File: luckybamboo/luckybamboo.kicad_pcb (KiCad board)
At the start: 4 copper layers, 70.7 x 53.3 mm, 153 parts, among them J1 NEIGHBOR1, J10 TEST_2P, J11 TEST_2P, J12 TEST_2P, J13 TEST_2P, J14 TEST_2P, J15 TEST_2P, J16 TEST_2P, J17 Conn_Coaxial, J18 Conn_Coaxial, J19 TEST_2P, J2 NEIGHBOR2, J20 TEST_2P, J21 TEST_2P, J22 TEST_2P, J23 TEST_2P, J24 TEST_2P, J25 TEST_2P, J26 TEST_2P, J27 TEST_2P, J28 TEST_2P, J29 TEST_2P, J3 Conn_01x08, J30 TEST_2P, J31 TEST_2P, J32 TEST_2P, J33 TEST_2P, J4 Conn_01x08, J5 Conn_01x08, J6 Conn_01x08, J7 BONUS_ROW, J8 TEST_2P, J9 TEST_2P, U1 ADF7242, U10 ADF7242_balun, U11 ADF7242_balun, U12 HHM2293A1, U13 BGA7H1N6, U14 ADF7242_balun, U15 ADF7242_balun, U16 ADF7242_balun, U17 ADF7242_balun, U2 ADF7242, U3 ADF7242, U4 ADF7242, U5 SKY13322, U6 HHM2293A1, U7 HHM2293A1, U8 ADF7242_balun, U9 ADF7242_balun, X1 XTAL4PIN, X2 XTAL4PIN, X3 XTAL4PIN, X4 XTAL4PIN

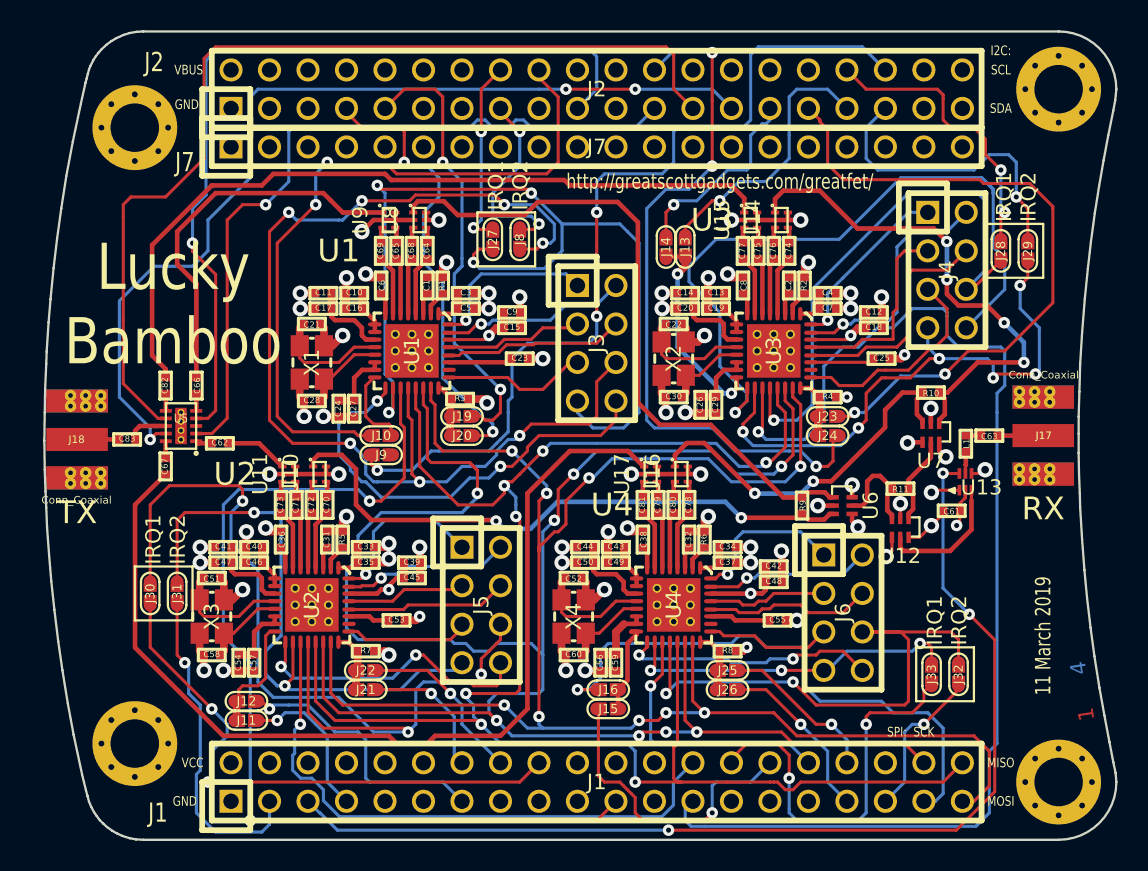
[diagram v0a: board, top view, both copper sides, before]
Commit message: Lucky Bamboo: Rerouted RX RF signals and rearranged schematic to be consistent with layout. Gladiolus: Routed incomplete signal near TX transistor.
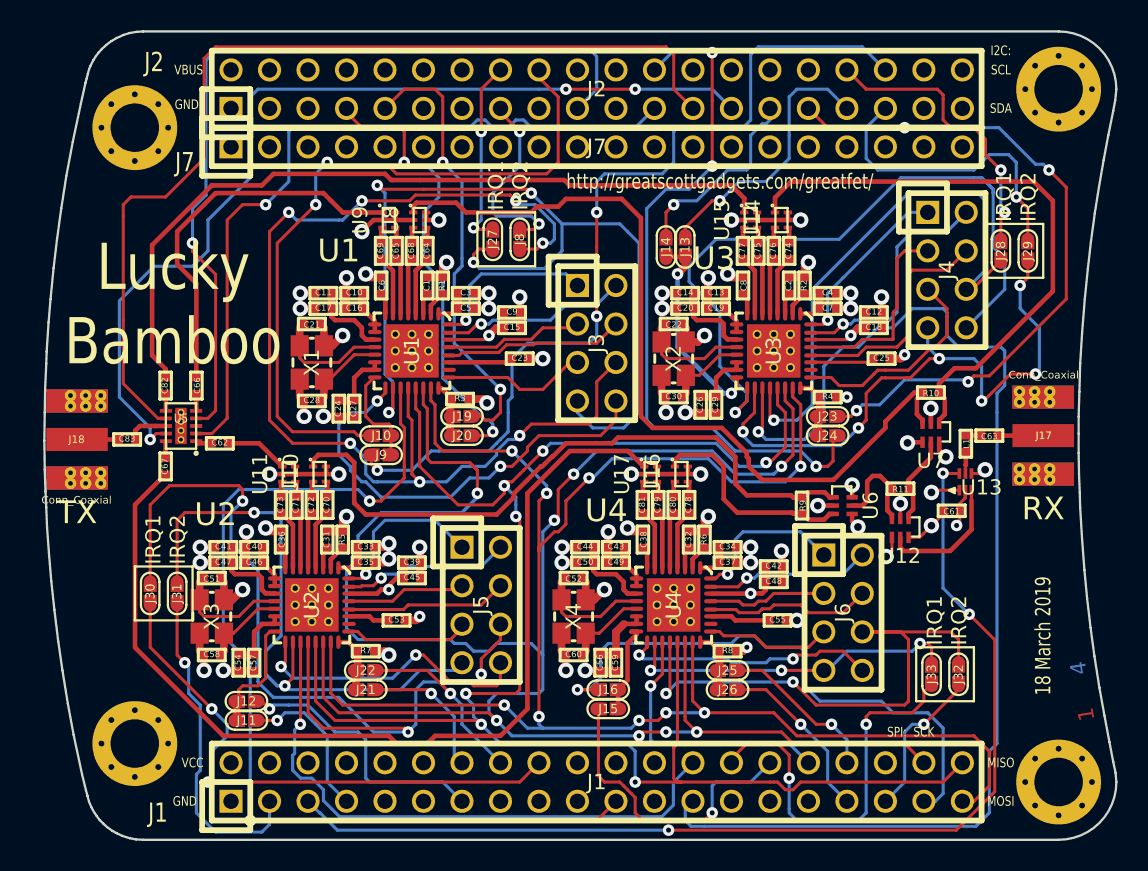
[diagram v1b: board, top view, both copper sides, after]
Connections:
- R10 pad 1: /RFIN4 -> /RFIN1
- R9 pad 1: /RFIN2 -> /RFIN4
- R9 pad 2: /RFIN1 -> /RFIN2
- U6 pad 1: /RFIN1 -> /RFIN2
- U6 pad 3: /RFIN2 -> /RFIN4
- U7 pad 3: /RFIN4 -> /RFIN1
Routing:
- net /RFIN1: track 44.3 -> 55.5 mm
- net /RFIN4: track 24.6 -> 14.2 mm, vias 2 -> 0
- net /RFIN3: track 33.8 -> 39.2 mm, vias 4 -> 0
- net /RFIN2: track 39.9 -> 43.3 mm, vias 2 -> 0
- net /TRFS3: track 38.3 -> 40.4 mm
- net /DR1: track 5.72 -> 6.99 mm
- net /P6_7: track 43.9 -> 45.0 mm, vias 2 -> 4
- net /P4_3: track 29.6 -> 30.2 mm
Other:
- board text added: "18 March 2019"
- board text removed: "11 March 2019"
